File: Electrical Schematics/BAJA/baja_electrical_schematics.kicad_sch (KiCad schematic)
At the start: 9 parts, among them SW1 SW_Nidec_CAS-120A1, SW2 SW_Nidec_CAS-120A1, SW3 SW_DPST, SW4 SW_Nidec_CAS-120A1, U1 BC95

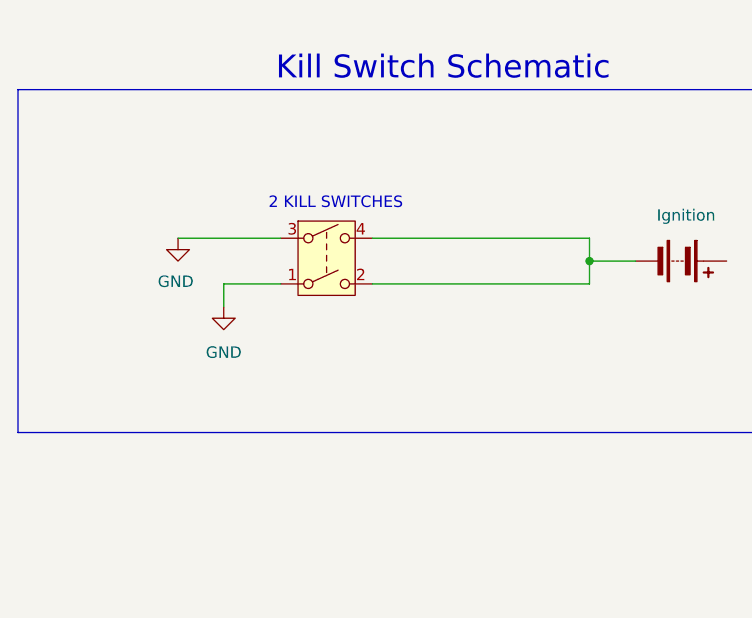
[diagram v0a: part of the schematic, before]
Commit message: Updated Baja Schematics (Updated Kill Switch)
Update kill switch schematic so that when the switch is pressed, it grounds the entire system but otherwise allows current through the kill switches
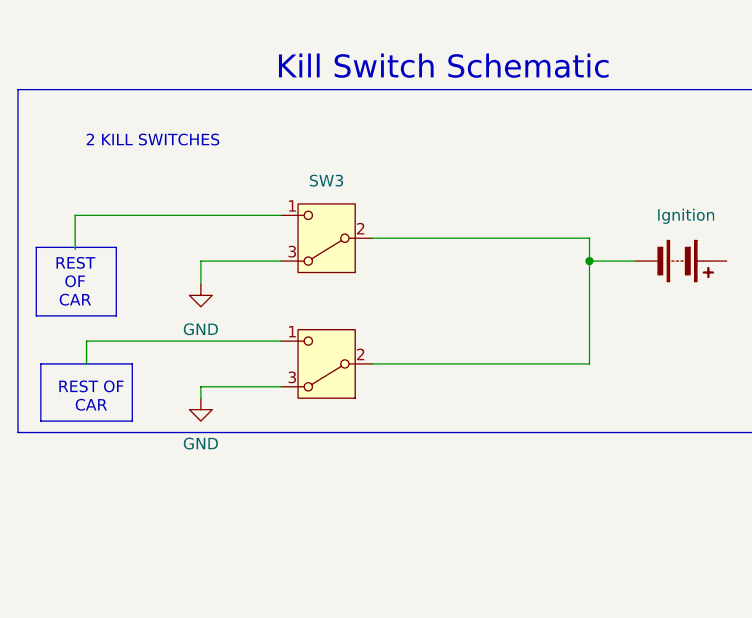
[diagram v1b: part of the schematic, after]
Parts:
- removed SW3: SW_DPST, symbol Switch:SW_DPST
- added SW3, SW5: SW_Nidec_CAS-120A1, Button_Switch_SMD:Nidec_Copal_CAS-120A, symbol Switch:SW_Nidec_CAS-120A1
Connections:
- net GND: now also SW3.3 (A), SW5.3 (A)
- net at BT1.2 (-): now also SW3.2 (B), SW5.2 (B)
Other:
- note added: "REST OF CAR"
